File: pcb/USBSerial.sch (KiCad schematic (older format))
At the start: 5 parts, among them P301 USB_OTG, Q301 FT230XS-R

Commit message: ready for etching!
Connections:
- net GND: now also P301.6 (shield)
- net at C301.2, Q301.3 (VCCIO): no longer Q301.10 (3V3OUT)
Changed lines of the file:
@@
 $EndComp
 $Comp
-L GND #PWR023
+L GND #PWR020
 U 1 1 56AD0F3F
 P 2700 2600
-F 0 "#PWR023" H 2700 2350 50  0001 C CNN
+F 0 "#PWR020" H 2700 2350 50  0001 C CNN
 F 1 "GND" H 2700 2450 50  0000 C CNN
 F 2 "" H 2700 2600 60  0000 C CNN
@@
 $EndComp
 $Comp
-L GND #PWR024
+L GND #PWR021
 U 1 1 56AD0F57
 P 2200 2900
-F 0 "#PWR024" H 2200 2650 50  0001 C CNN
+F 0 "#PWR021" H 2200 2650 50  0001 C CNN
 F 1 "GND" H 2200 2750 50  0000 C CNN
 F 2 "" H 2200 2900 60  0000 C CNN
@@
 Wire Wire Line
 	4600 1500 4600 1650
-Wire Wire Line
-	3800 1500 3800 1950
 $Comp
 L C C301
@@
 $EndComp
 $Comp
-L GND #PWR025
+L GND #PWR022
 U 1 1 56AD1283
 P 3600 2000
-F 0 "#PWR025" H 3600 1750 50  0001 C CNN
+F 0 "#PWR022" H 3600 1750 50  0001 C CNN
 F 1 "GND" H 3600 1850 50  0000 C CNN
 F 2 "" H 3600 2000 60  0000 C CNN
@@
 	3700 2750 3800 2750
 $Comp
-L GND #PWR026
+L GND #PWR023
 U 1 1 56AD15C9
 P 4600 3100
-F 0 "#PWR026" H 4600 2850 50  0001 C CNN
+F 0 "#PWR023" H 4600 2850 50  0001 C CNN
 F 1 "GND" H 4600 2950 50  0000 C CNN
 F 2 "" H 4600 3100 60  0000 C CNN
@@
 $EndComp
 $Comp
-L GND #PWR027
+L GND #PWR024
 U 1 1 56AD15F7
 P 4400 3100
-F 0 "#PWR027" H 4400 2850 50  0001 C CNN
+F 0 "#PWR024" H 4400 2850 50  0001 C CNN
 F 1 "GND" H 4400 2950 50  0000 C CNN
 F 2 "" H 4400 3100 60  0000 C CNN
@@
 Wire Wire Line
 	3600 1500 4600 1500
-Connection ~ 3800 1500
 Wire Wire Line
 	2600 2600 2700 2600
+Wire Wire Line
+	2200 2800 2200 2900
 $EndSCHEMATC

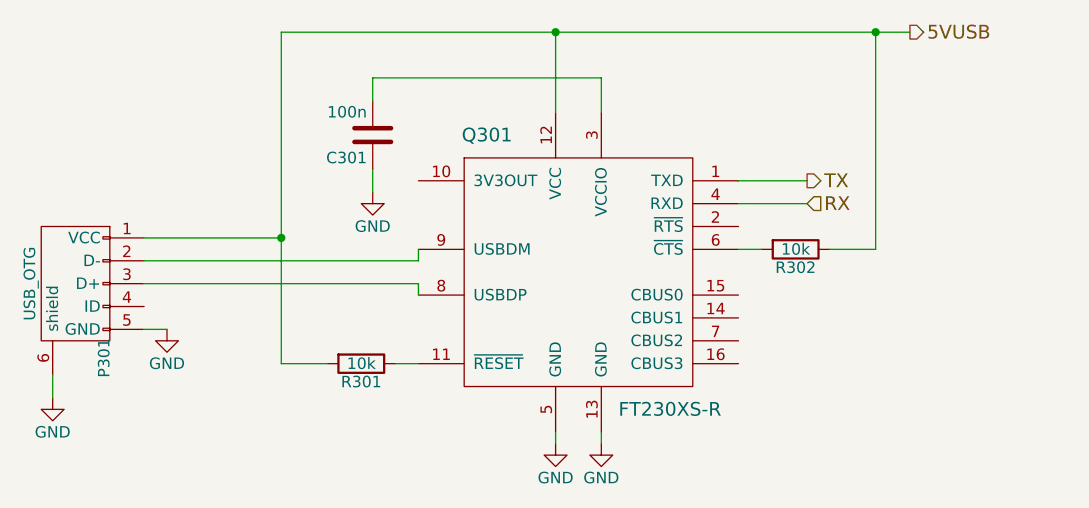
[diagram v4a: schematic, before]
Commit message: removed resistor dividors, added cap to usb
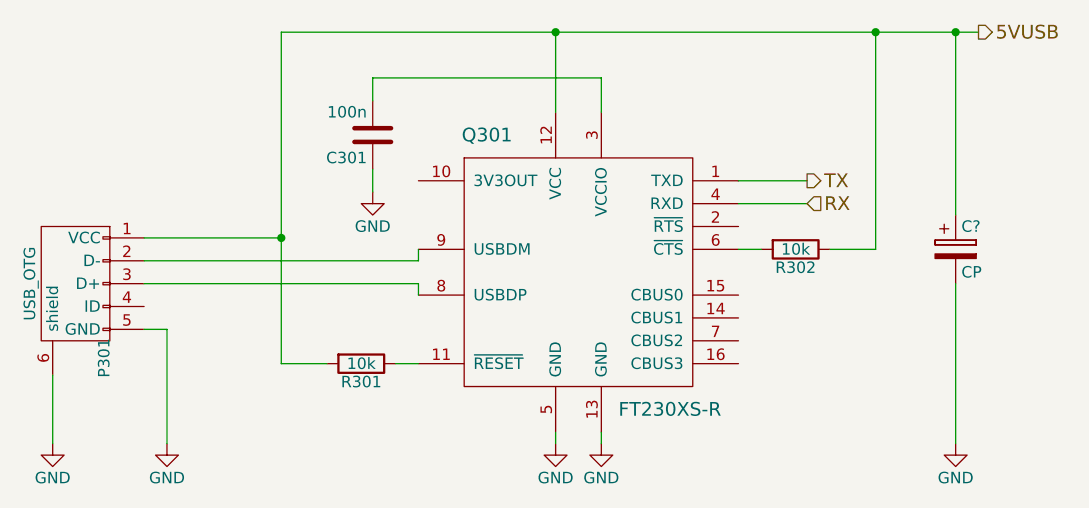
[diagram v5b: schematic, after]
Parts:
- added C?: CP, symbol CP
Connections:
- net 5VUSB: now also C?.1
- net GND: now also C?.2
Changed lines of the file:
@@
 $EndComp
 $Comp
-L GND #PWR302
+L GND #PWR030
 U 1 1 56AD0F3F
-P 2700 2600
-F 0 "#PWR302" H 2700 2350 50  0001 C CNN
-F 1 "GND" H 2700 2450 50  0000 C CNN
-F 2 "" H 2700 2600 60  0000 C CNN
-F 3 "" H 2700 2600 60  0000 C CNN
-	1    2700 2600
+P 2700 3100
+F 0 "#PWR030" H 2700 2850 50  0001 C CNN
+F 1 "GND" H 2700 2950 50  0000 C CNN
+F 2 "" H 2700 3100 60  0000 C CNN
+F 3 "" H 2700 3100 60  0000 C CNN
+	1    2700 3100
 	1    0    0    -1
 $EndComp
 $Comp
-L GND #PWR301
+L GND #PWR031
 U 1 1 56AD0F57
-P 2200 2900
-F 0 "#PWR301" H 2200 2650 50  0001 C CNN
-F 1 "GND" H 2200 2750 50  0000 C CNN
-F 2 "" H 2200 2900 60  0000 C CNN
-F 3 "" H 2200 2900 60  0000 C CNN
-	1    2200 2900
+P 2200 3100
+F 0 "#PWR031" H 2200 2850 50  0001 C CNN
+F 1 "GND" H 2200 2950 50  0000 C CNN
+F 2 "" H 2200 3100 60  0000 C CNN
+F 3 "" H 2200 3100 60  0000 C CNN
+	1    2200 3100
 	1    0    0    -1
 $EndComp
@@
 $EndComp
 $Comp
-L GND #PWR303
+L GND #PWR032
 U 1 1 56AD1283
 P 3600 2000
-F 0 "#PWR303" H 3600 1750 50  0001 C CNN
+F 0 "#PWR032" H 3600 1750 50  0001 C CNN
 F 1 "GND" H 3600 1850 50  0000 C CNN
 F 2 "" H 3600 2000 60  0000 C CNN
@@
 	3700 2750 3800 2750
 $Comp
-L GND #PWR305
+L GND #PWR033
 U 1 1 56AD15C9
 P 4600 3100
-F 0 "#PWR305" H 4600 2850 50  0001 C CNN
+F 0 "#PWR033" H 4600 2850 50  0001 C CNN
 F 1 "GND" H 4600 2950 50  0000 C CNN
 F 2 "" H 4600 3100 60  0000 C CNN
@@
 $EndComp
 $Comp
-L GND #PWR304
+L GND #PWR034
 U 1 1 56AD15F7
 P 4400 3100
-F 0 "#PWR304" H 4400 2850 50  0001 C CNN
+F 0 "#PWR034" H 4400 2850 50  0001 C CNN
 F 1 "GND" H 4400 2950 50  0000 C CNN
 F 2 "" H 4400 3100 60  0000 C CNN
@@
 	4400 1650 4400 1300
 Wire Wire Line
-	3200 1300 5950 1300
+	3200 1300 4400 1300
 Wire Wire Line
-	3200 1300 3200 2750
+	4400 1300 5800 1300
+Wire Wire Line
+	5800 1300 6150 1300
+Wire Wire Line
+	6150 1300 6250 1300
+Wire Wire Line
+	3200 1300 3200 2200
+Wire Wire Line
+	3200 2200 3200 2750
 Wire Wire Line
 	5800 1300 5800 2250
@@
 Wire Wire Line
 	5200 2250 5300 2250
-Text HLabel 5950 1300 2    60   Output ~ 0
+Text HLabel 6250 1300 2    60   Output ~ 0
 5VUSB
 Connection ~ 5800 1300
@@
 	2600 2600 2700 2600
 Wire Wire Line
-	2200 2800 2200 2900
+	2700 2600 2700 3100
+Wire Wire Line
+	2200 2800 2200 3100
+$Comp
+L CP C?
+U 1 1 570E4572
+P 6150 2250
+F 0 "C?" H 6175 2350 50  0000 L CNN
+F 1 "CP" H 6175 2150 50  0000 L CNN
+F 2 "" H 6188 2100 50  0000 C CNN
+F 3 "" H 6150 2250 50  0000 C CNN
+	1    6150 2250
+	1    0    0    -1
+$EndComp
+$Comp
+L GND #PWR?
+U 1 1 570E46BD
+P 6150 3100
+F 0 "#PWR?" H 6150 2850 50  0001 C CNN
+F 1 "GND" H 6150 2950 50  0000 C CNN
+F 2 "" H 6150 3100 50  0000 C CNN
+F 3 "" H 6150 3100 50  0000 C CNN
+	1    6150 3100
+	1    0    0    -1
+$EndComp
+Wire Wire Line
+	6150 3100 6150 2400
+Wire Wire Line
+	6150 1300 6150 2100
+Connection ~ 6150 1300
 $EndSCHEMATC

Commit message: added mcu
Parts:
- C302: renamed from C?; footprint (none) -> Capacitors_SMD:c_elec_8x5.4
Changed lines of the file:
@@
 $EndComp
 $Comp
-L GND #PWR030
+L GND #PWR026
 U 1 1 56AD0F3F
 P 2700 3100
-F 0 "#PWR030" H 2700 2850 50  0001 C CNN
+F 0 "#PWR026" H 2700 2850 50  0001 C CNN
 F 1 "GND" H 2700 2950 50  0000 C CNN
 F 2 "" H 2700 3100 60  0000 C CNN
@@
 $EndComp
 $Comp
-L GND #PWR031
+L GND #PWR027
 U 1 1 56AD0F57
 P 2200 3100
-F 0 "#PWR031" H 2200 2850 50  0001 C CNN
+F 0 "#PWR027" H 2200 2850 50  0001 C CNN
 F 1 "GND" H 2200 2950 50  0000 C CNN
 F 2 "" H 2200 3100 60  0000 C CNN
@@
 $EndComp
 $Comp
-L GND #PWR032
+L GND #PWR028
 U 1 1 56AD1283
 P 3600 2000
-F 0 "#PWR032" H 3600 1750 50  0001 C CNN
+F 0 "#PWR028" H 3600 1750 50  0001 C CNN
 F 1 "GND" H 3600 1850 50  0000 C CNN
 F 2 "" H 3600 2000 60  0000 C CNN
@@
 	3700 2750 3800 2750
 $Comp
-L GND #PWR033
+L GND #PWR029
 U 1 1 56AD15C9
 P 4600 3100
-F 0 "#PWR033" H 4600 2850 50  0001 C CNN
+F 0 "#PWR029" H 4600 2850 50  0001 C CNN
 F 1 "GND" H 4600 2950 50  0000 C CNN
 F 2 "" H 4600 3100 60  0000 C CNN
@@
 $EndComp
 $Comp
-L GND #PWR034
+L GND #PWR030
 U 1 1 56AD15F7
 P 4400 3100
-F 0 "#PWR034" H 4400 2850 50  0001 C CNN
+F 0 "#PWR030" H 4400 2850 50  0001 C CNN
 F 1 "GND" H 4400 2950 50  0000 C CNN
 F 2 "" H 4400 3100 60  0000 C CNN
@@
 	4400 1650 4400 1300
 Wire Wire Line
-	3200 1300 4400 1300
+	3200 1300 6250 1300
 Wire Wire Line
-	4400 1300 5800 1300
-Wire Wire Line
-	5800 1300 6150 1300
-Wire Wire Line
-	6150 1300 6250 1300
-Wire Wire Line
-	3200 1300 3200 2200
-Wire Wire Line
-	3200 2200 3200 2750
+	3200 1300 3200 2750
 Wire Wire Line
 	5800 1300 5800 2250
@@
 	2200 2800 2200 3100
 $Comp
-L CP C?
+L CP C302
 U 1 1 570E4572
 P 6150 2250
-F 0 "C?" H 6175 2350 50  0000 L CNN
+F 0 "C302" H 6175 2350 50  0000 L CNN
 F 1 "CP" H 6175 2150 50  0000 L CNN
-F 2 "" H 6188 2100 50  0000 C CNN
+F 2 "Capacitors_SMD:c_elec_8x5.4" H 6188 2100 50  0001 C CNN
 F 3 "" H 6150 2250 50  0000 C CNN
 	1    6150 2250
@@
 $EndComp
 $Comp
-L GND #PWR?
+L GND #PWR031
 U 1 1 570E46BD
 P 6150 3100
-F 0 "#PWR?" H 6150 2850 50  0001 C CNN
+F 0 "#PWR031" H 6150 2850 50  0001 C CNN
 F 1 "GND" H 6150 2950 50  0000 C CNN
 F 2 "" H 6150 3100 50  0000 C CNN
